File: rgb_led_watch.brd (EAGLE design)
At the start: 50 x 50 mm, 30 parts, among them IC4 74V1T126CTR

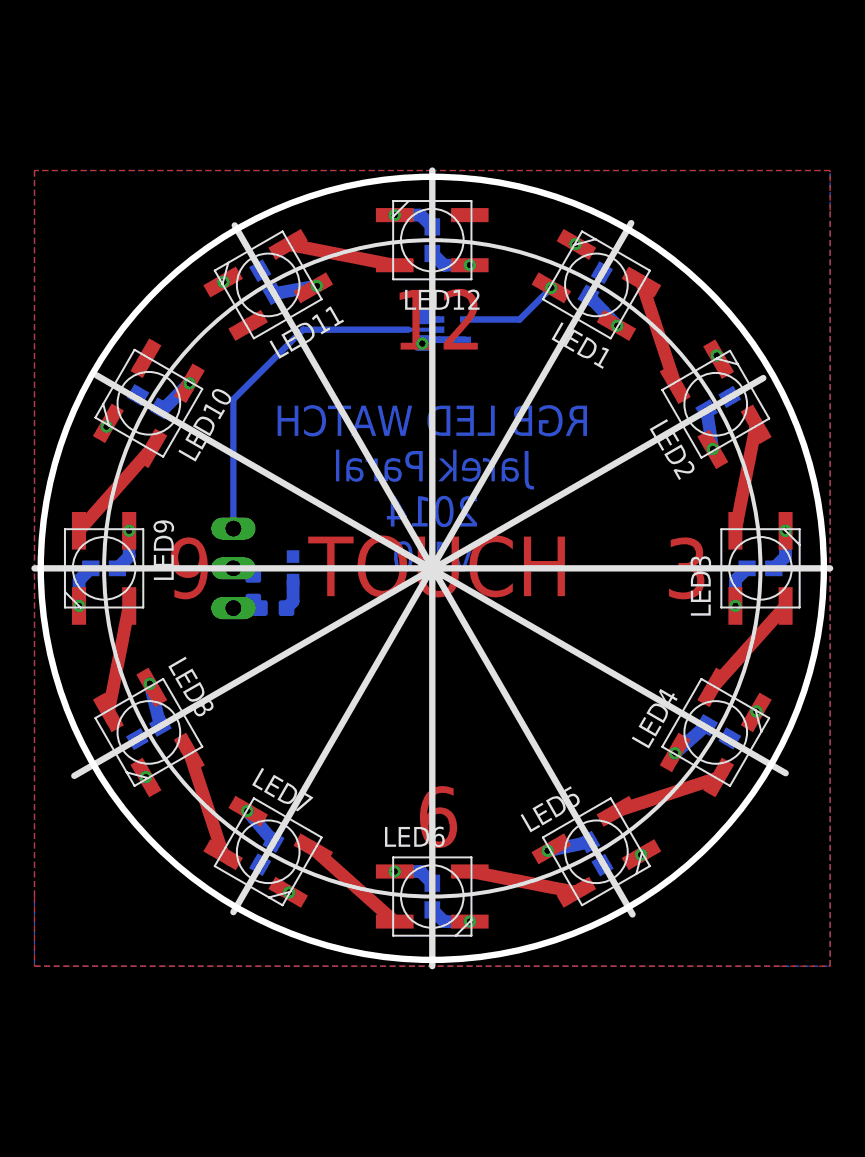
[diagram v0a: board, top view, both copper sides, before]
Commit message: v1.1: opraveny chyby (nezaroutovana draha, spatne nastaveni polygonu)
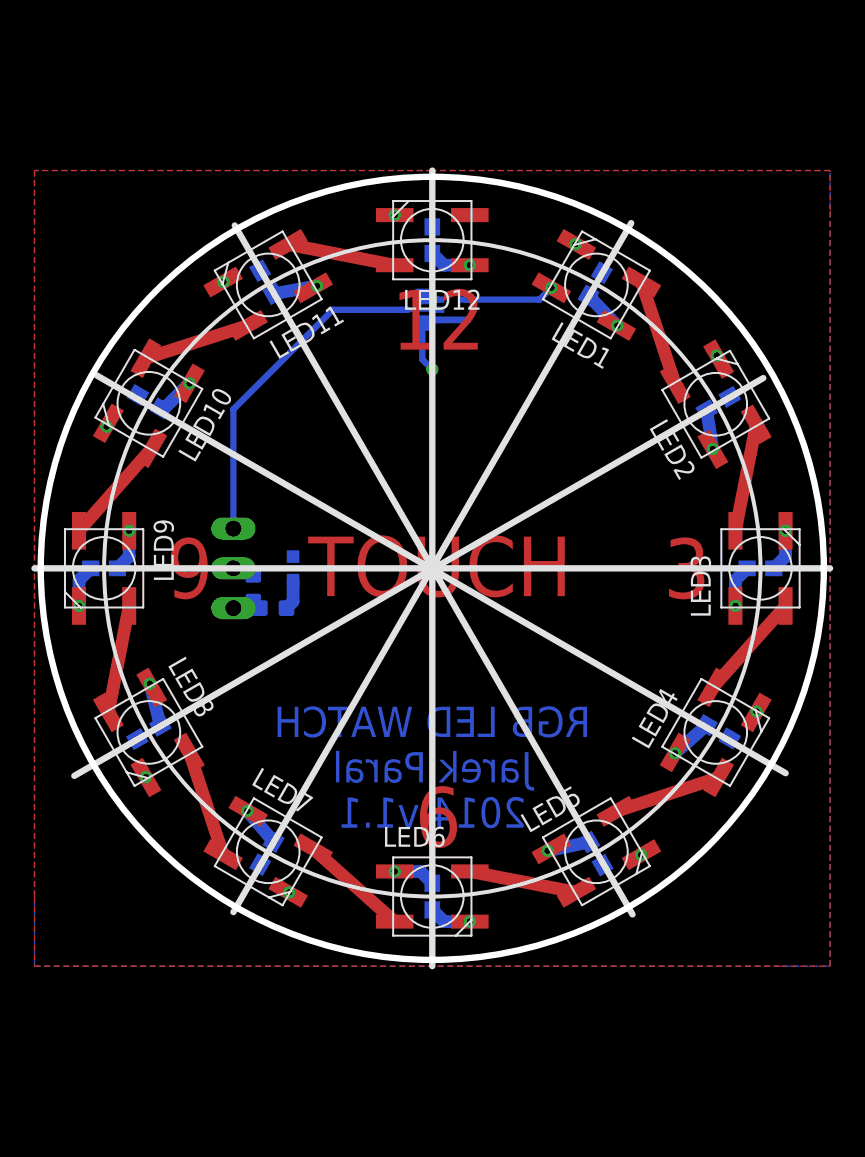
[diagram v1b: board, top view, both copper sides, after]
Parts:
- moved C14 1.27 mm to (50.2, 67.3)
- moved IC4 1.27 mm to (52.1, 67.3)
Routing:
- net N$9: track 0.00 -> 6.85 mm
- net +5V: track 40.2 -> 43.4 mm
- net GND: track 13.4 -> 10.7 mm
- net SIG_OUT: track 6.32 -> 5.79 mm
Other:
- board text added: "RGB LED WATCH Jarek Paral 2014 v1.1"
- board text removed: "RGB LED WATCH Jarek Paral 2014 v1.0"
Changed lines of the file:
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@@
 <setting verticaltext="up"/>
 </settings>
-<grid distance="0.025" unitdist="inch" unit="inch" style="lines" multiple="1" display="yes" altdistance="0.005" altunitdist="inch" altunit="inch"/>
+<grid distance="0.025" unitdist="inch" unit="mm" style="lines" multiple="1" display="yes" altdistance="0.005" altunitdist="inch" altunit="inch"/>
 <layers>
 <layer number="1" name="Top" color="4" fill="1" visible="yes" active="yes"/>
@@
 <wire x1="63.5" y1="72.842634375" x2="38.099996875" y2="28.84854375" width="0.4064" layer="21"/>
 <wire x1="71.935725" y1="62.950071875" x2="27.941634375" y2="37.550071875" width="0.4064" layer="21"/>
-<text x="50.8" y="55.88" size="1.9304" layer="16" font="vector" ratio="20" rot="MR0" align="center">RGB LED WATCH
+<text x="50.8" y="38.1" size="1.9304" layer="16" font="vector" ratio="20" rot="MR0" align="center">RGB LED WATCH
 Jarek Paral
-2014
-v1.0</text>
+2014 v1.1</text>
 <text x="51.308" y="49.022" size="3.81" layer="1" font="vector" ratio="20" align="bottom-center">TOUCH</text>
 <text x="51.181" y="64.77" size="3.81" layer="1" font="vector" ratio="20" align="bottom-center">12</text>
@@
 <element name="LED13" library="led" package="CHIPLED_0603" value="GREEN" x="41.91" y="50.8" rot="MR0"/>
 <element name="C13" library="rcl_upravena" package="C0603" value="4u7" x="39.37" y="49.53" rot="MR90"/>
-<element name="C14" library="rcl_upravena" package="C0603" value="100n/6,3V" x="50.165" y="66.04" rot="MR270"/>
-<element name="IC4" library="74xx-little-de" package="SC70-5" value="74V1T126CTR " x="52.07" y="66.04" rot="MR90"/>
+<element name="C14" library="rcl_upravena" package="C0603" value="100n/6,3V" x="50.165" y="67.31" rot="MR270"/>
+<element name="IC4" library="74xx-little-de" package="SC70-5" value="74V1T126CTR " x="52.07" y="67.31" rot="MR90"/>
 </elements>
 <signals>
@@
 <contactref element="LED12" pad="VSS"/>
 <contactref element="C12" pad="1"/>
-<wire x1="50.8" y1="72.605" x2="50.05" y2="73.355" width="0.8128" layer="16"/>
-<wire x1="50.05" y1="73.355" x2="48.4" y2="73.355" width="0.8128" layer="16"/>
 <via x="48.4" y="73.355" extent="1-16" drill="0.4"/>
-<polygon width="0.8128" layer="16" isolate="0.762">
+<polygon width="0.5" layer="16" isolate="0.3">
 <vertex x="50.8" y="76.2"/>
 <vertex x="25.4" y="76.2"/>
@@
 <contactref element="JP1" pad="2"/>
 <contactref element="C13" pad="2"/>
-<wire x1="51.22" y1="66.69" x2="50.365" y2="66.69" width="0.4064" layer="16"/>
-<wire x1="50.365" y1="66.69" x2="50.165" y2="66.89" width="0.4064" layer="16"/>
+<wire x1="51.22" y1="67.96" x2="50.365" y2="67.96" width="0.4064" layer="16"/>
+<wire x1="50.365" y1="67.96" x2="50.165" y2="68.16" width="0.4064" layer="16"/>
 <wire x1="39.37" y1="50.38" x2="38.95" y2="50.8" width="0.8128" layer="16"/>
 <wire x1="38.95" y1="50.8" x2="38.1" y2="50.8" width="0.8128" layer="16"/>
@@
 <via x="53.2" y="70.155" extent="1-16" drill="0.4"/>
 <via x="35.306" y="62.611" extent="1-16" drill="0.4"/>
-<polygon width="0.8128" layer="1" isolate="0.762">
+<polygon width="0.5" layer="1" isolate="0.3">
 <vertex x="50.8" y="76.2"/>
 <vertex x="25.4" y="76.2"/>
@@
 <contactref element="C13" pad="1"/>
 <contactref element="IC4" pad="1"/>
-<wire x1="51.22" y1="65.39" x2="50.365" y2="65.39" width="0.4064" layer="16"/>
+<wire x1="51.22" y1="66.66" x2="50.365" y2="66.66" width="0.4064" layer="16"/>
 <wire x1="38.1" y1="48.26" x2="39.79" y2="48.26" width="0.8128" layer="16"/>
 <wire x1="39.37" y1="48.68" x2="39.79" y2="48.26" width="0.8128" layer="16"/>
-<wire x1="52.92" y1="65.39" x2="51.22" y2="65.39" width="0.4064" layer="16"/>
-<wire x1="50.365" y1="65.39" x2="50.165" y2="65.19" width="0.4064" layer="16"/>
-<wire x1="52.92" y1="65.39" x2="50.15" y2="65.39" width="0.4064" layer="16"/>
-<wire x1="50.15" y1="65.39" x2="50.165" y2="65.151" width="0.4064" layer="16"/>
-<via x="50.165" y="65.151" extent="1-16" drill="0.4"/>
+<wire x1="52.92" y1="66.66" x2="51.22" y2="66.66" width="0.4064" layer="16"/>
+<wire x1="50.365" y1="66.66" x2="50.165" y2="66.46" width="0.4064" layer="16"/>
+<wire x1="52.92" y1="66.66" x2="50.165" y2="66.66" width="0.4064" layer="16"/>
+<wire x1="50.165" y1="66.66" x2="50.15" y2="66.66" width="0.4064" layer="16"/>
+<via x="50.8" y="63.5" extent="1-16" drill="0.4"/>
+<wire x1="50.165" y1="66.66" x2="50.165" y2="64.135" width="0.4064" layer="16"/>
+<wire x1="50.165" y1="64.135" x2="50.8" y2="63.5" width="0.4064" layer="16"/>
 <wire x1="62.555959375" y1="66.31185625" x2="62.611" y2="66.294" width="0" layer="19" extent="1-1"/>
 <wire x1="35.288140625" y1="62.6182375" x2="35.288140625" y2="62.6182375" width="0" layer="19" extent="1-16"/>
@@
 <wire x1="58.166" y1="32.766" x2="58.3990375" y2="32.888140625" width="0" layer="19" extent="1-1"/>
 <wire x1="32.766" y1="43.434" x2="32.888140625" y2="43.200959375" width="0" layer="19" extent="1-1"/>
-<wire x1="51.22" y1="65.39" x2="51.55" y2="70.155" width="0" layer="19" extent="16-16"/>
 </signal>
 <signal name="N$3">
@@
 <contactref element="LED11" pad="DIN"/>
 <contactref element="LED10" pad="DOUT"/>
-<wire x1="32.51685625" y1="64.2182375" x2="39.0440375" y2="66.31185625" width="0" layer="19" extent="1-1"/>
+<wire x1="32.51685625" y1="64.2182375" x2="39.0440375" y2="66.31185625" width="0.8128" layer="1"/>
 </signal>
 <signal name="N$10">
@@
 <contactref element="IC4" pad="4"/>
 <contactref element="LED1" pad="DIN"/>
-<wire x1="52.92" y1="66.69" x2="56.37718125" y2="66.69" width="0.4064" layer="16"/>
-<wire x1="56.37718125" y1="66.69" x2="58.3990375" y2="68.71185625" width="0.4064" layer="16"/>
+<wire x1="52.92" y1="67.96" x2="57.64718125" y2="67.96" width="0.4064" layer="16"/>
+<wire x1="57.64718125" y1="67.96" x2="58.3990375" y2="68.71185625" width="0.4064" layer="16"/>
 <via x="58.3990375" y="68.71185625" extent="1-16" drill="0.4"/>
 </signal>
@@
 <contactref element="IC4" pad="2"/>
 <contactref element="JP1" pad="1"/>
-<wire x1="38.1" y1="53.34" x2="38.1" y2="61.595" width="0.4064" layer="16"/>
-<wire x1="38.1" y1="61.595" x2="42.545" y2="66.04" width="0.4064" layer="16"/>
-<wire x1="42.545" y1="66.04" x2="49.276" y2="66.04" width="0.4064" layer="16"/>
-<wire x1="49.276" y1="66.04" x2="51.22" y2="66.04" width="0.254" layer="16"/>
+<wire x1="38.1" y1="53.34" x2="38.1" y2="60.96" width="0.4064" layer="16"/>
+<wire x1="38.1" y1="60.96" x2="44.45" y2="67.31" width="0.4064" layer="16"/>
+<wire x1="44.45" y1="67.31" x2="49.276" y2="67.31" width="0.4064" layer="16"/>
+<wire x1="49.276" y1="67.31" x2="51.22" y2="67.31" width="0.254" layer="16"/>
 </signal>
 </signals>

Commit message: v1.2: pridan kapacitni senzor
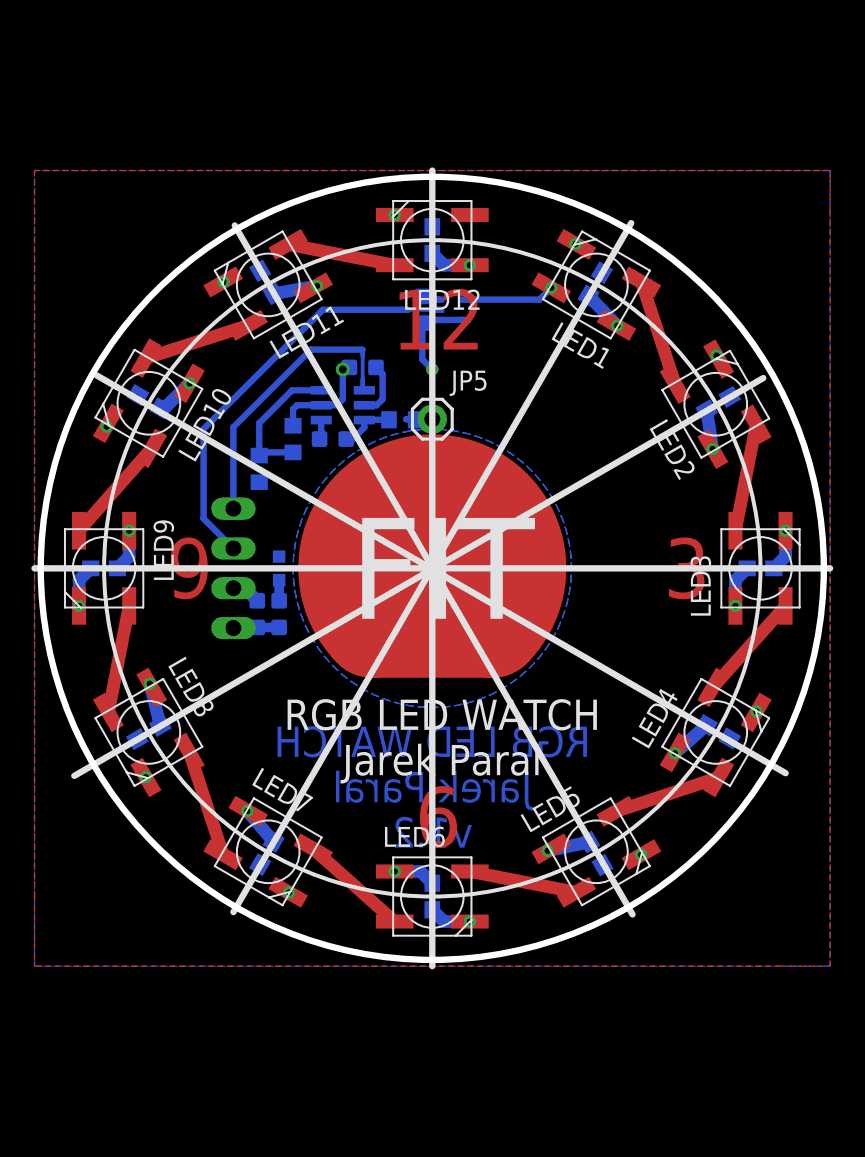
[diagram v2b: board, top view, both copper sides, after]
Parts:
- added C15: 10n, rcl_upravena:C0603
- added C16: 100n/6,3V, rcl_upravena:C0603
- added JP5: M01PTH, SparkFun-Connectors:1X01
- added R1: 10k, rcl:R0603
- added R2_LOW, R3_FAST: 0, rcl:R0603
- added U1: AT42QT1010SOT23, SparkFun-DigitalIC:SOT23-6
- JP1: device pinhead:1X03/90 -> pinhead:1X04/90
- moved C13 1.67 mm to (39.6, 47.9)
- moved LED13 0.89 mm to (41.0, 50.8)
- moved R4 0.54 mm to (41.0, 47.9), turned to 90 degrees
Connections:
- new net PAD: JP5.1, R1.2
- new net SNS: C15.2, U1.4
- new net SNSK: C15.1, R1.1, U1.3
- new net SWITCH: JP1.1, U1.1
- new net SYNC_MODE: R2_LOW.2, R3_FAST.1, U1.6
- net +5V: now also C16.1, JP1.4, R3_FAST.2, U1.5; no longer JP1.3
- net GND: now also C16.2, JP1.3, R2_LOW.1, U1.2; no longer JP1.2
- net SIG_IN: now also JP1.2; no longer JP1.1
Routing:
- net PAD: track 0.00 -> 44.9 mm
- net SWITCH: track 0.00 -> 19.1 mm
- net SYNC_MODE: track 0.00 -> 9.14 mm
- net +5V: track 43.4 -> 48.2 mm, vias 13 -> 14
- net GND: track 10.7 -> 14.7 mm
- net SNSK: track 0.00 -> 3.52 mm
- net SIG_IN: track 23.4 -> 26.6 mm
- net SNS: track 0.00 -> 1.22 mm
- net N$2: track 1.96 -> 1.32 mm
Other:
- board text added: "AT42QT1010"
- board text added: "Breakout"
- board text added: "FIT"
- board text added: "RGB LED WATCH Jarek Paral"
- board text added: "RGB LED WATCH Jarek Paral v1.2"
- board text removed: "RGB LED WATCH Jarek Paral 2014 v1.1"
- board text removed: "TOUCH"

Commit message: v1.3: upraven tvar do podoby hodinek (pridelany ouska) - pripraveno do vyroby
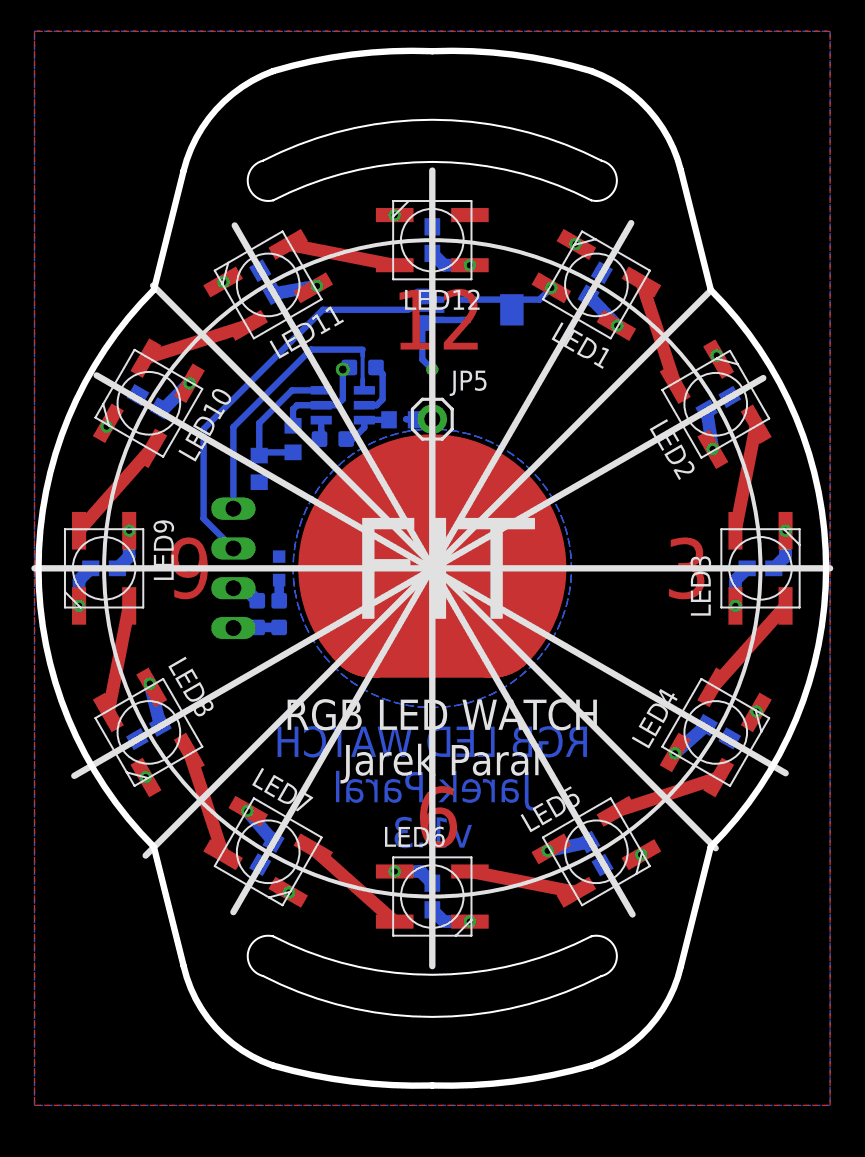
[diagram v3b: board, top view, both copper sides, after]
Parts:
- added JP9: M01SMD-4.5X1.5, SparkFun-Connectors:PAD-1.5X4.5
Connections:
- net SIG_OUT: now also JP9.P$1
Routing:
- net +5V: track 48.2 -> 52.4 mm
- net GND: track 14.7 -> 16.0 mm
- net SIG_OUT: track 5.79 -> 6.44 mm
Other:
- board size 50 x 50 mm -> 50.3 x 66.1 mm
- board text added: "RGB LED WATCH Jarek Paral v1.3"
- board text removed: "RGB LED WATCH Jarek Paral v1.2"

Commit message: hodinky
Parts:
- removed C14, C16: 100n/6,3V, rcl_upravena:C0603
- removed C15: 10n, rcl_upravena:C0603
- removed IC4: 74V1T126CTR, 74xx-little-de:SC70-5
- removed JP1: (no value), pinhead:1X04/90
- removed JP5: M01PTH, SparkFun-Connectors:1X01
- removed JP9: M01SMD-4.5X1.5, SparkFun-Connectors:PAD-1.5X4.5
- removed R1: 10k, rcl:R0603
- removed R2_LOW, R3_FAST: 0, rcl:R0603
- removed U1: AT42QT1010SOT23, SparkFun-DigitalIC:SOT23-6
- added C17, C18, C19, C20: 100nF, rcl_upravena:C0306
- added C21, C22: 10nF, rcl_upravena:C0805
- added L1: 10uH, rcl_upravena:R0805
- added L2: FB, rcl_upravena:R0603
- added LED14: WS2812B, rgb_led:WS2812B
- added U$1: CON_PROG-6CORN, con_prog:SMD-6-CORNER
- added U$2: ATXMEGA128A4U_AU, xmega:TQFP44
- C13: value 4u7 -> 100n; device rcl_upravena:C0603 -> resistor:C0603
- moved C13 11.2 mm to (50.8, 47.6), flipped to the top, turned to 0 degrees
- moved C9 3.61 mm to (33.4, 51.4)
- moved LED9 3.61 mm to (33.4, 51.4)
- moved C11 3.59 mm to (42.1, 66.0)
- moved C2 3.53 mm to (66.0, 59.5)
- moved C3 3.49 mm to (68.3, 51.4)
- moved LED3 3.49 mm to (68.3, 51.4)
- moved C10 3.49 mm to (35.7, 59.5)
- moved C7 3.49 mm to (41.9, 35.7), turned to 300 degrees
- moved C4 3.47 mm to (66.0, 42.0)
- moved C12 3.43 mm to (50.8, 68.3)
- moved C6 3.43 mm to (50.8, 33.3)
- moved LED12 3.43 mm to (50.8, 68.3)
- moved LED6 3.43 mm to (50.8, 33.3)
- moved LED10 3.42 mm to (35.6, 59.6)
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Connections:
- removed net PAD: JP5.1, R1.2
- removed net SIG_IN: IC4.2, JP1.2
- removed net SNS: C15.2, U1.4
- removed net SNSK: C15.1, R1.1, U1.3
- removed net SWITCH: JP1.1, U1.1
- removed net SYNC_MODE: R2_LOW.2, R3_FAST.1, U1.6
- new net +3V3: L1.1, U$1.P$2
- new net N$1: C17.2, C18.2, C19.2, C21.2, L1.2, L2.1
- new net N$11: C20.1, C22.1, L2.2, U$2.39
- new net N$12: U$1.P$1, U$2.34
- new net N$13: U$1.P$3, U$2.33
- new net N$14: U$1.P$4, U$2.32
- new net N$15: U$1.P$5, U$2.35
- new net N$16: LED12.DOUT, LED14.DIN
- net +5V: now also C13.2, LED14.VDD; no longer C13.1, C14.2, C16.1, IC4.1, IC4.5, JP1.4, R3_FAST.2, U1.5
- net GND: now also C13.1, C17.1, C18.1, C19.1, C20.2, C21.1, C22.2, LED14.VSS, U$1.P$6, U$2.18, U$2.19, U$2.30, U$2.31, U$2.38, U$2.8, U$2.9; no longer C13.2, C14.1, C16.2, IC4.3, JP1.3, R2_LOW.1, U1.2
- net SIG_OUT: now also U$2.23; no longer IC4.4, JP9.P$1
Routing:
- net PAD: track 44.9 -> 0.00 mm
- net SIG_IN: track 26.6 -> 0.00 mm
- net GND: track 16.0 -> 42.1 mm
- net SWITCH: track 19.1 -> 0.00 mm
- net +5V: track 52.4 -> 37.6 mm, vias 14 -> 12
- net SYNC_MODE: track 9.14 -> 0.00 mm
- net SIG_OUT: track 6.44 -> 0.00 mm
- net SNSK: track 3.52 -> 0.00 mm
- net N$5: track 6.93 -> 4.81 mm
- net LED2: track 7.02 -> 4.92 mm
- net N$10: track 6.93 -> 5.35 mm
- net N$7: track 6.87 -> 5.33 mm
- net N$4: track 6.87 -> 5.33 mm
- net LED1: track 6.97 -> 5.45 mm
- net N$6: track 6.93 -> 5.47 mm
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- added copper zone on layer 1, net GND
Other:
- board text removed: "AT42QT1010"
- board text removed: "Breakout"
- board text removed: "RGB LED WATCH Jarek Paral v1.3"
